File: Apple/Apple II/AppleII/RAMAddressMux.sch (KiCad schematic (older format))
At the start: 15 parts, among them J1 74LS257

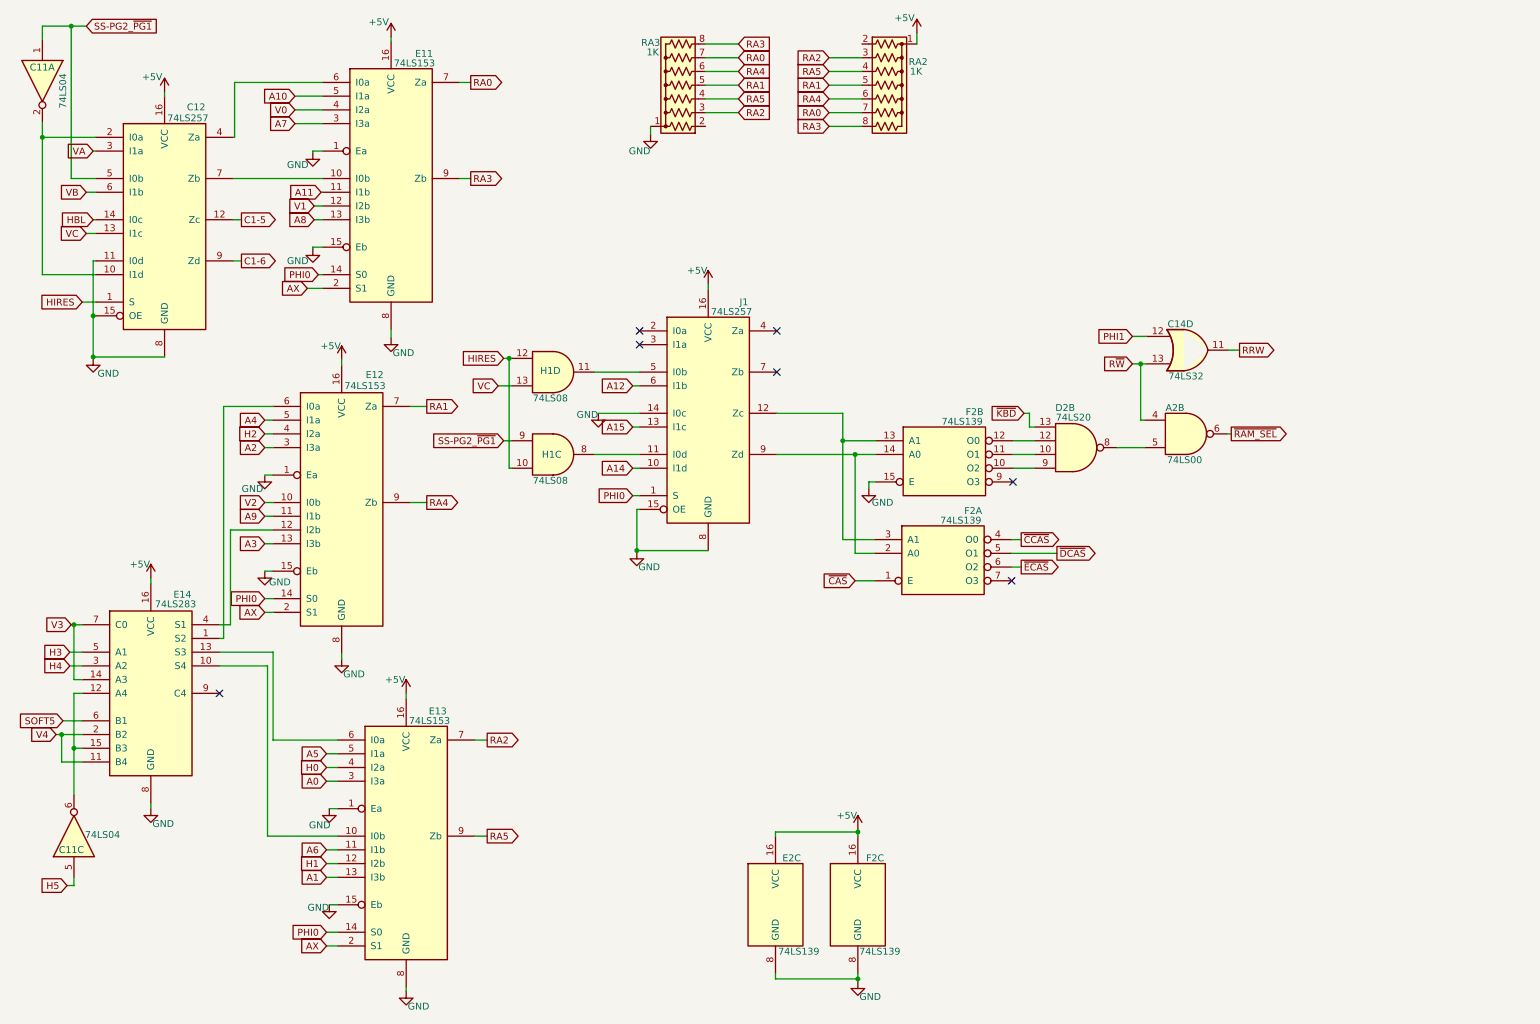
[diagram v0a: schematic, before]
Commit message: Created separate II and II+ projects, stated updating the II+
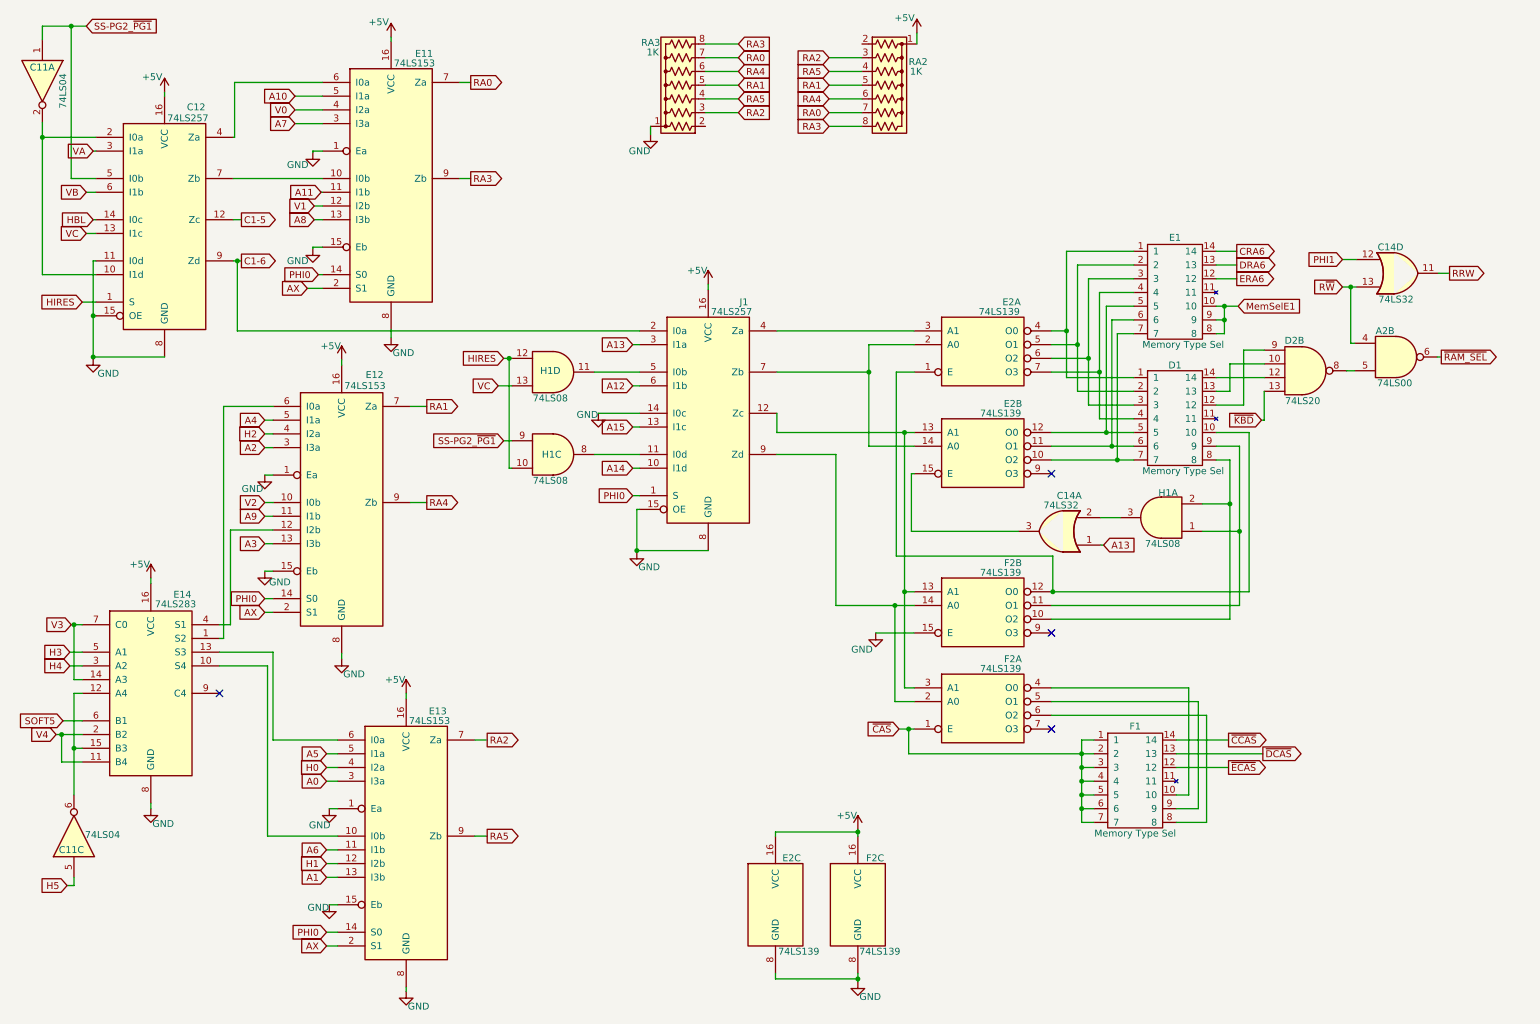
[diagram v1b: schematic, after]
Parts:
- added unit 1 of C14
- added D1, E1, F1: Memory Type Sel, symbol AppleII+:AppII_MemorySelectBlock
- added unit 1 of E2
- added unit 2 of E2
- added unit 1 of H1
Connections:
- net C1-6: now also J1.2 (I0a)
- net ~CAS: now also F1.1, F1.2, F1.3, F1.4, F1.5, F1.6, F1.7
- net ~CCAS: now also F1.14; no longer F2.4 (O0)
- net ~DCAS: now also F1.13; no longer F2.5 (O1)
- net ~ECAS: now also F1.12; no longer F2.6 (O2)
- net at F2.13 (A1), F2.3 (A1), J1.12 (Zc): now also E2.13 (A1)
- net A13: now reaches J1.3 (I1a)
- net A13: now also C14.1
- net at J1.4 (Za): now also E2.3 (A1)
- net at J1.7 (Zb): now also E2.14 (A0), E2.2 (A0)
- net at F2.10 (O2): now also D1.8, H1.2; no longer D2.9
- net at F2.11 (O1): now also D1.9, H1.1; no longer D2.10
- net at F2.12 (O0): now also D1.10, E2.1 (E); no longer D2.12
- new net: F1.10, F2.4 (O0)
- new net: F1.9, F2.5 (O1)
- new net: F1.8, F2.6 (O2)
- new net: D1.1, E1.1, E2.4 (O0)
- new net: D1.2, E1.2, E2.5 (O1)
- new net: D1.3, E1.3, E2.6 (O2)
- new net: D1.4, E1.4, E2.7 (O3)
- new net: D1.7, E1.7, E2.10 (O2)
- new net: D1.6, E1.6, E2.11 (O1)
- new net: D1.5, E1.5, E2.12 (O0)
- new net: C14.3, E2.15 (E)
- new net: C14.2, H1.3
- new net: D1.13, D2.10
- new net: D1.14, D2.12
- new net: D1.12, D2.9
- new net CRA6: E1.14
- new net DRA6: E1.13
- new net ERA6: E1.12
- new net MemSelE1: E1.10, E1.8, E1.9
- no-connect marks 7 -> 4
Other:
- moved on the sheet: A2B, C14D, D2B, F2A, F2B
